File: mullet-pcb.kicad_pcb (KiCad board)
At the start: 2 copper layers, 299.7 x 97.7 mm, 187 parts, among them SW1 KEYSW, SW10 KEYSW, SW11 KEYSW, SW12 KEYSW, SW13 KEYSW, SW14 KEYSW, SW15 KEYSW, SW16 KEYSW, SW17 KEYSW, SW18 KEYSW, SW19 KEYSW, SW2 KEYSW, SW20 KEYSW, SW21 KEYSW, SW22 KEYSW, SW23 KEYSW, SW24 KEYSW, SW25 KEYSW, SW26 KEYSW, SW27 KEYSW, SW28 KEYSW, SW29 KEYSW, SW3 KEYSW, SW30 KEYSW, SW31 KEYSW, SW32 KEYSW, SW33 KEYSW, SW34 KEYSW, SW35 KEYSW, SW36 KEYSW, SW37 KEYSW, SW38 KEYSW, SW39 KEYSW, SW4 KEYSW, SW40 KEYSW, SW41 KEYSW, SW42 KEYSW, SW43 KEYSW, SW44 KEYSW, SW45 KEYSW, SW46 KEYSW, SW47 KEYSW, SW48 KEYSW, SW49 KEYSW, SW5 KEYSW, SW50 KEYSW, SW51 KEYSW, SW52 KEYSW, SW53 KEYSW, SW54 KEYSW, SW55 KEYSW, SW56 KEYSW, SW57 KEYSW, SW58 KEYSW, SW59 KEYSW, SW6 KEYSW, SW60 KEYSW, SW61 KEYSW, SW62 KEYSW, SW63 KEYSW, SW64 KEYSW, SW65 KEYSW, SW66 KEYSW, SW67 KEYSW, SW7 KEYSW, SW8 KEYSW, SW9 KEYSW, U1 ATMEGA32U4, U2 PRTR5V0U2X, X1 XTAL_GND

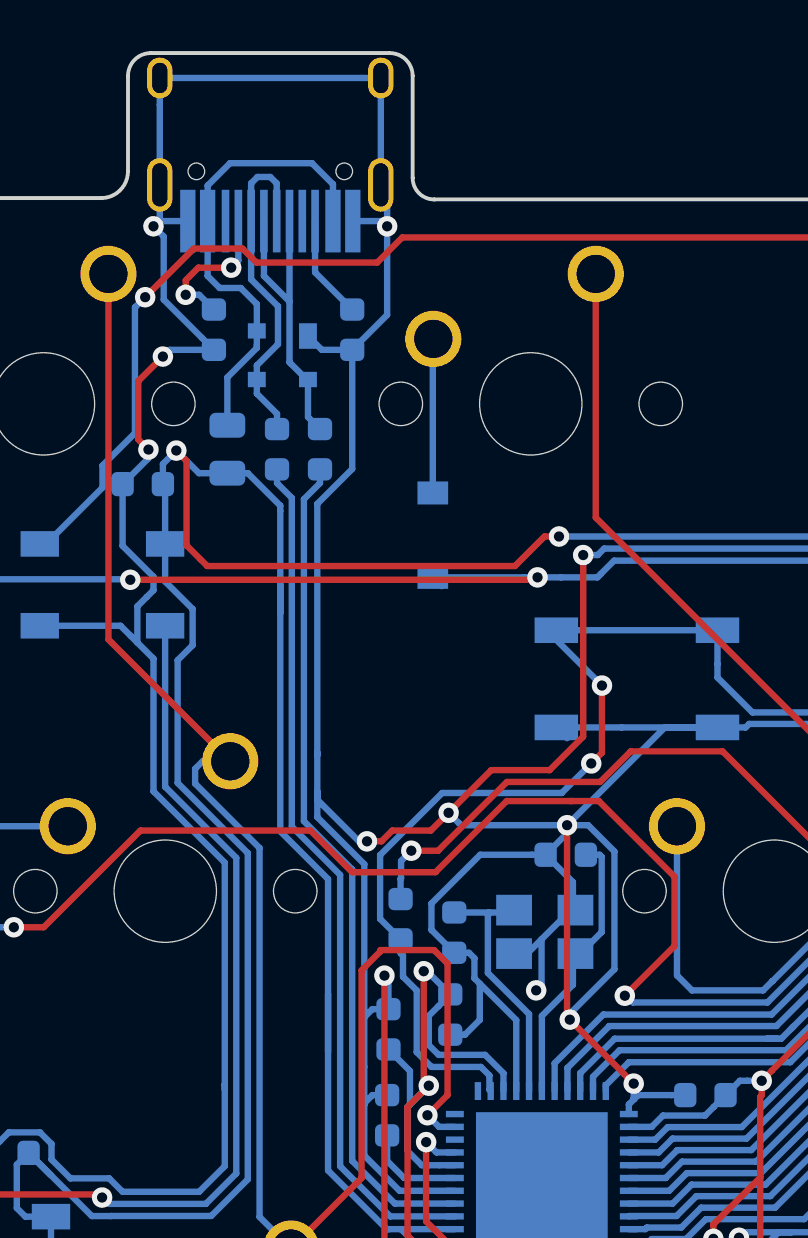
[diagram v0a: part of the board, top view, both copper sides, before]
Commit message: update ground fills for usb and xtal
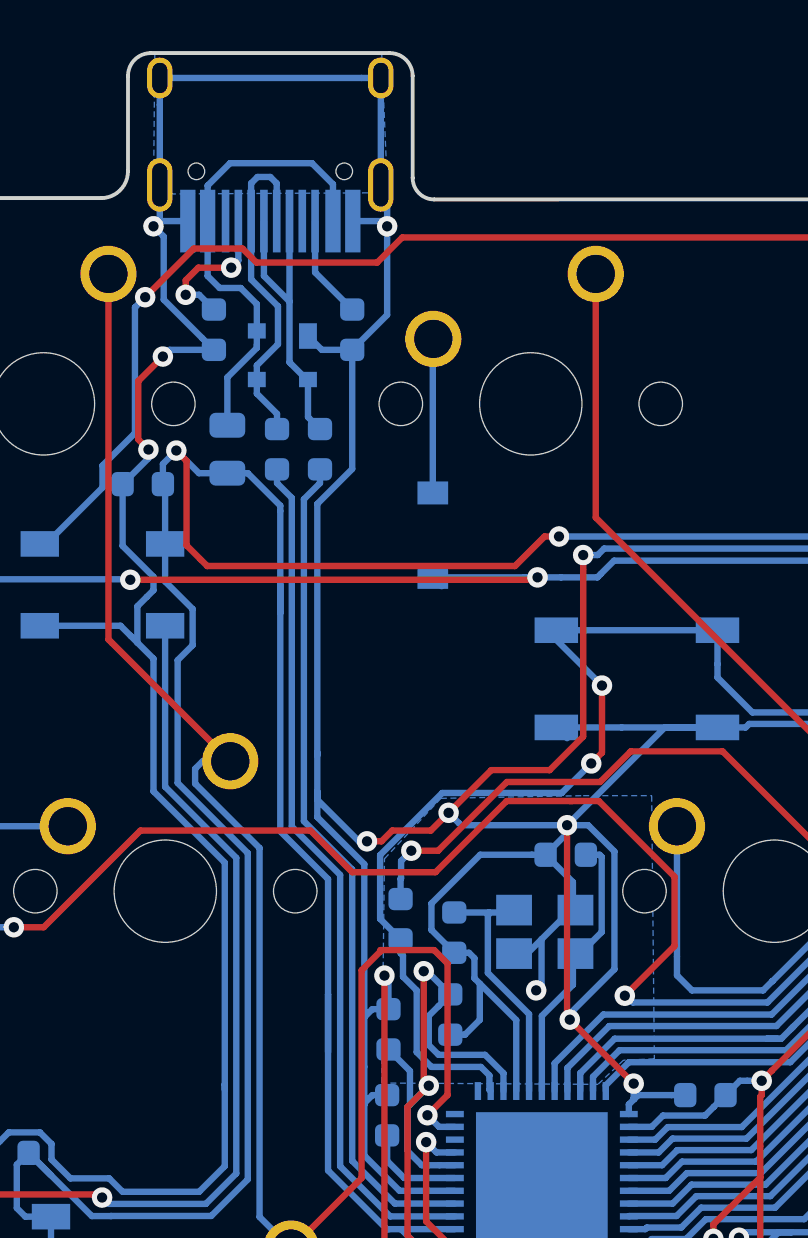
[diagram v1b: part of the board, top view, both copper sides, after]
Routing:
- added copper zone on B.Cu, net GND
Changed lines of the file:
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@@
     (last_trace_width 0.25)
     (trace_clearance 0.2)
-    (zone_clearance 0.508)
+    (zone_clearance 0.4)
     (zone_45_only no)
     (trace_min 0.2)
@@
       )
     )
+  )
+  (zone (net 1) (net_name GND) (layer B.Cu) (hatch edge 0.508)
+    (connect_pads (clearance 0.508))
+    (min_thickness 0.254)
+    (fill yes (arc_segments 16) (thermal_gap 0.508) (thermal_bridge_width 0.508))
+    (polygon
+      (pts
+        (xy 11.338488 0.839888) (xy 20.209805 0.944874) (xy 20.419777 5.984202) (xy 20.419777 6.351653) (xy 11.285995 6.404146)
+      )
+    )
+  )
+  (zone (net 1) (net_name GND) (layer B.Cu) (hatch edge 0.508)
+    (connect_pads (clearance 0.4))
+    (min_thickness 0.254)
+    (fill yes (arc_segments 16) (thermal_gap 0.508) (thermal_bridge_width 0.508))
+    (polygon
+      (pts
+        (xy 20.314791 32.388181) (xy 22.519497 30.025996) (xy 28.083755 29.92101) (xy 30.760898 29.92101) (xy 30.865884 40.209638)
+        (xy 29.658545 40.262131) (xy 28.661178 41.207005) (xy 20.209805 41.154512)
+      )
+    )
